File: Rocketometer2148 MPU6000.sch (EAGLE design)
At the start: 75 parts, among them J001 USB_MICROB_JST, J301 JST 2mm, J401 M06, J402 M06, J701 MICROSD-SOCKET, Q050 PMOS, Q201 PMOS, U101 BMP180, U201 5319, U301 73831, U401 LPC2148, U402 SN74LVC1G32, U501 L3G4200D, U801 5883, U901 LIS331, U902 AD377, Y401 12MHz, Y402 32kiHz

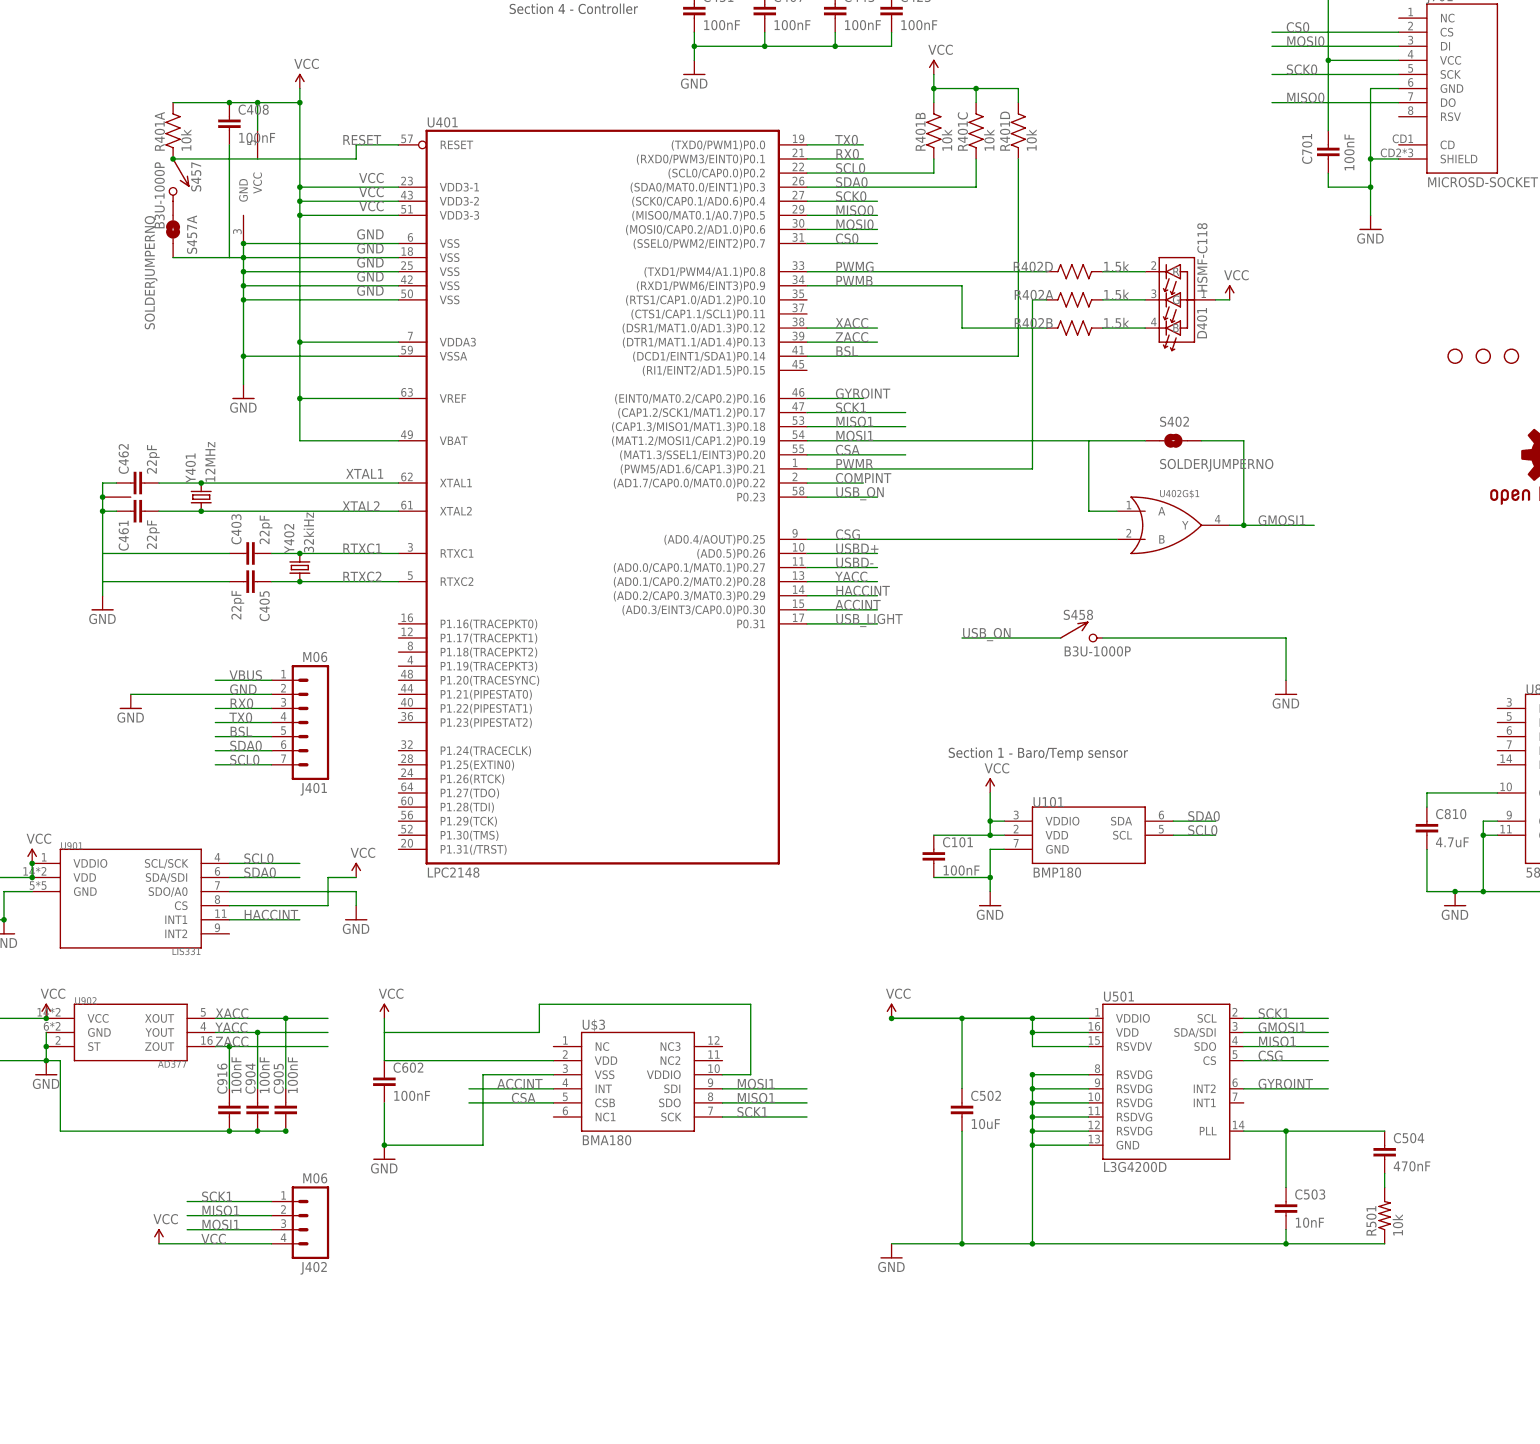
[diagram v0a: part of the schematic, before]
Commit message: Made 11DoF for BMA180, MPU6000, replaced ADXL345 with BMA180 in Rocketometer2148, made Rocketometer2148 with MPU6000
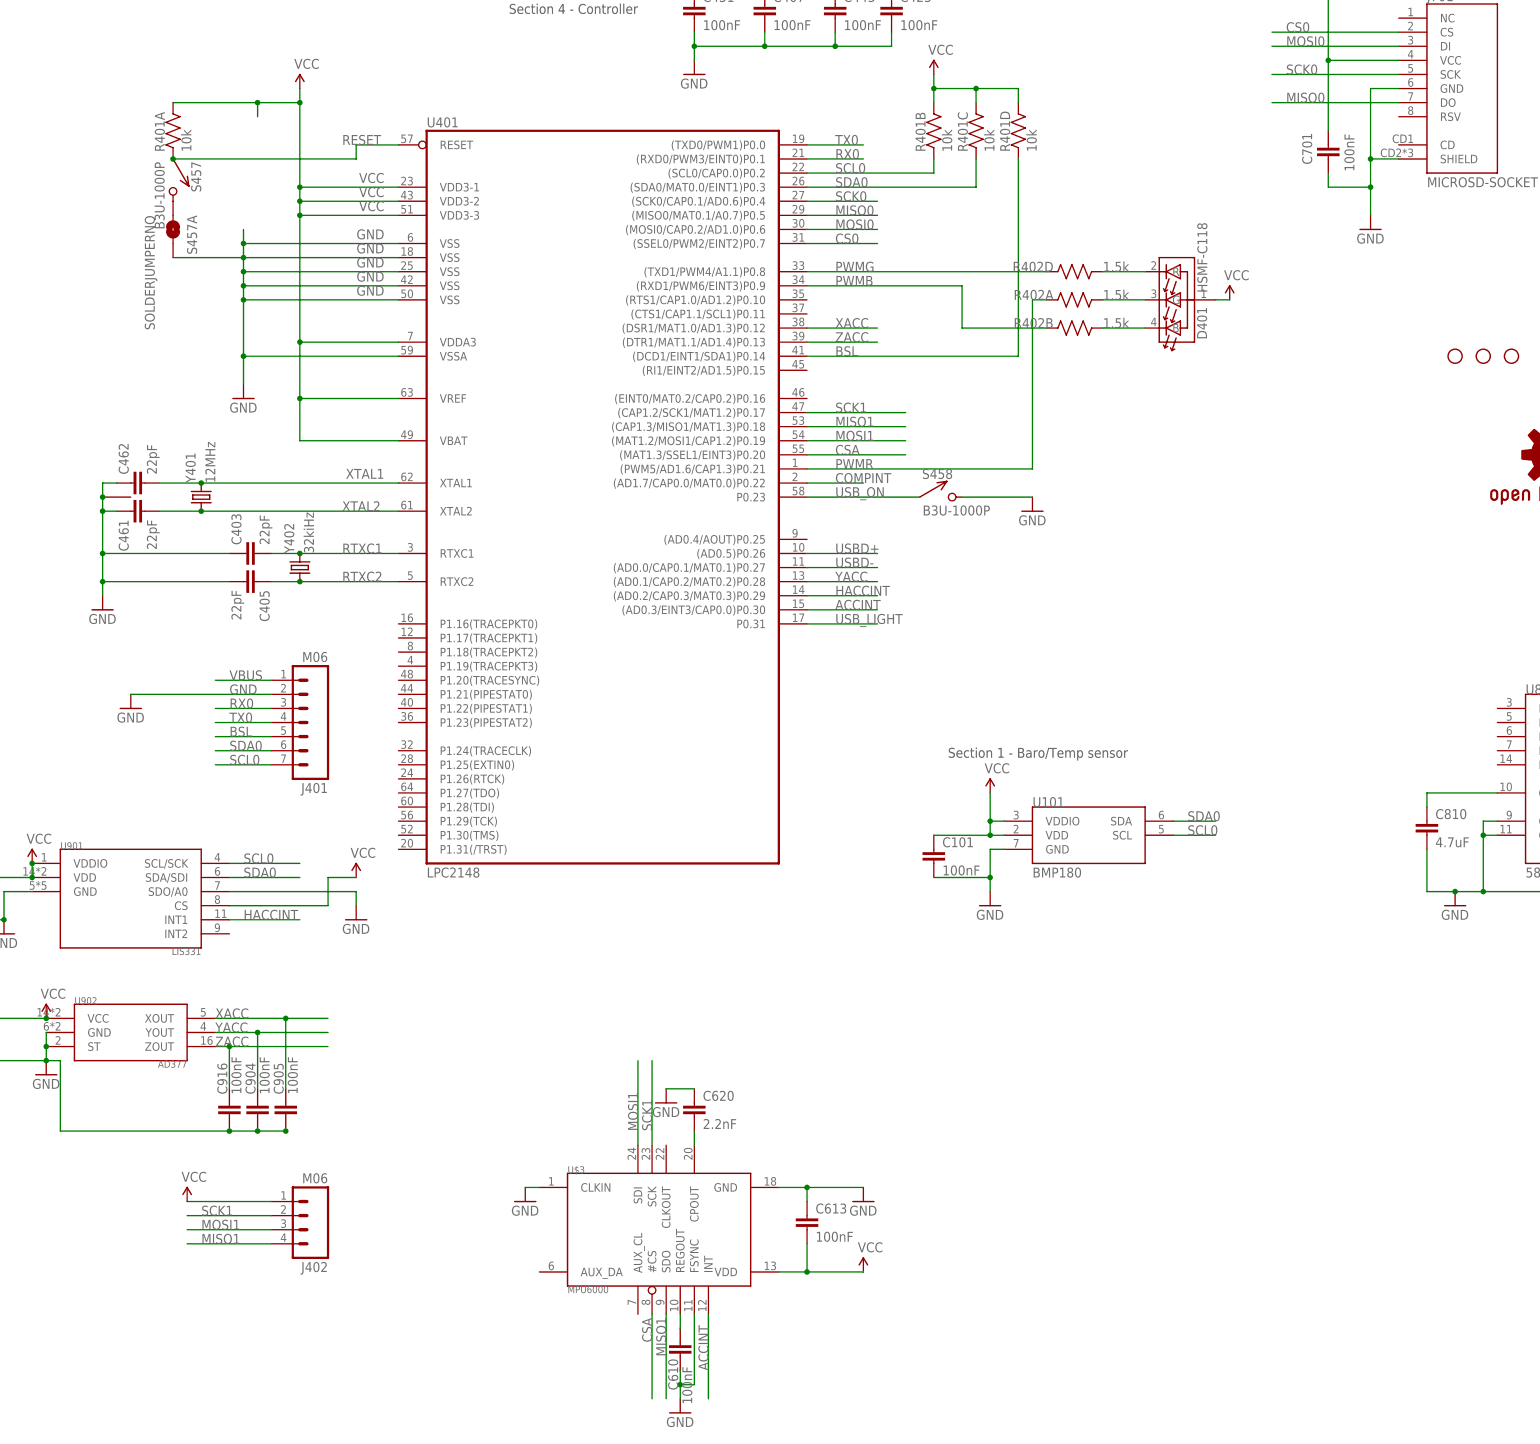
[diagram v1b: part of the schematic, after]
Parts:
- removed C408, C602: 100nF, SparkFun:CAP0402-CAP
- removed C502: 10uF, SparkFun:CAP0603-CAP
- removed C503: 10nF, SparkFun:CAP0402-CAP
- removed C504: 470nF, SparkFun:CAP0402-CAP
- removed R501: 10k, SparkFun:RESISTOR0402-RES
- removed S402: SOLDERJUMPERNO, SparkFun-Passives:SOLDERJUMPERNO
- removed U402: SN74LVC1G32, KwanSystems:SN74LVC1G32
- removed U501: L3G4200D, SparkFun:L3G4200D
- added C610, C613: 100nF, SparkFun:CAP0402-CAP
- added C620: 2.2nF, SparkFun:CAP0402-CAP
- D050: DIGIKEY 754-1434-1-ND -> 350-2037-1-ND
- D301: DIGIKEY 754-1354-1-ND -> 754-1124-1-ND
- U$3: value BMA180 -> MPU6000; device SparkFun-Sensors:BMA180 -> KwanSystems:MPU6000
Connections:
- removed net CSG: U401.(AD0.4/AOUT)P0.25, U402G$1.B, U501.CS
- removed net GMOSI1: S402.2, U402G$1.Y, U501.SDA/SDI
- removed net GYROINT: U401.(EINT0/MAT0.2/CAP0.2)P0.16, U501.INT2
- removed net N$20: C503.1, C504.1, U501.PLL
- new net N$13: C610.1, U$3.REGOUT
- net CSA: now also U$3.#CS; no longer U$3.CSB
- net GND: now also C610.2, C613.1, C620.1, U$3.CLKIN, U$3.FSYNC, U$3.GND; no longer C408.2, C502.2, C503.2, C602.2, R501.1, U$3.VSS, U402G$2.GND, U501.GND, U501.RSDVG@3, U501.RSVDG@0, U501.RSVDG@1, U501.RSVDG@2, U501.RSVDG@4
- net MISO1: now also J402.4; no longer J402.2, U501.SDO
- net MOSI1: no longer S402.1, U402G$1.A
- net N$1: now also C620.2, U$3.CPOUT; no longer C504.2, R501.2
- net SCK1: now also J402.2; no longer J402.1, U501.SCL
- net VCC: now also C613.2, J402.1; no longer C408.1, C502.1, C602.1, J402.4, U$3.VDDIO, U402G$2.VCC, U501.RSVDV@0, U501.VDD, U501.VDDIO
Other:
- moved on the sheet: S458

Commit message: Split off hardware stack initialization and checking
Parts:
- removed C904, C905, C916: 100nF, SparkFun:CAP0402-CAP
- removed C914: 4.7uF, SparkFun:CAP0402-CAP
- removed Q201: PMOS, SparkFun:MOSFET-PCHANNELSMD
- removed U902: AD377, KwanSystems:ADXL377
- added C449, C463: 100nF, SparkFun:CAP0402-CAP
- J401: device SparkFun-Connectors:M07 -> SparkFun-Connectors:M08LOCK
- J402: device SparkFun-Connectors:M04PTH -> SparkFun-Connectors:M04LOCK
- renumbered C201 to C215, C203 to C214
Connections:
- removed net RAW: C204.1, Q201.D, U201.EN, U201.VIN
- removed net XACC: C905.1, U401.(DSR1/MAT1.0/AD1.3)P0.12, U902.XOUT
- removed net YACC: C904.1, U401.(AD0.1/CAP0.2/MAT0.2)P0.28, U902.YOUT
- removed net ZACC: C916.1, U401.(DTR1/MAT1.1/AD1.4)P0.13, U902.ZOUT
- net BSL: now also J401.6; no longer J401.5
- net GND: now also C449.1, C463.2, J401.3, S201.S; no longer C904.2, C905.2, C914.2, C916.2, J401.2, S201.O, U902.GND, U902.ST
- net N$10: now also U201.EN; no longer Q201.G
- net RX0: now also J401.4; no longer J401.3
- net SCL0: now also J401.8; no longer J401.7
- net SDA0: now also J401.7; no longer J401.6
- net TX0: now also J401.5; no longer J401.4
- net VBUS: now also J401.2; no longer J401.1
- net VCC: now also C463.1; no longer C914.1, U401.VBAT, U902.VCC
- net VIN: now also C204.1, S201.O, U201.VIN; no longer Q201.S, S201.S
- net VLIPO: now also C449.2, J401.1, U401.VBAT
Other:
- moved on the sheet: R401A, S201, S457, S457A

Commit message: Finished routing of board
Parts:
- removed C901: 10uF, SparkFun:CAP0603-CAP
- removed U901: LIS331, KwanSystems:H3LIS331DL
- added C904, C905, C916: 100nF, SparkFun:CAP0402-CAP
- added C914: 4.7uF, SparkFun:CAP0402-CAP
- added U902: AD377, KwanSystems:ADXL377
- renumbered JP3 to JP5
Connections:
- new net XACC: C905.1, U401.(DSR1/MAT1.0/AD1.3)P0.12, U902.XOUT
- new net YACC: C904.1, U401.(AD0.1/CAP0.2/MAT0.2)P0.28, U902.YOUT
- new net ZACC: C916.1, U401.(DTR1/MAT1.1/AD1.4)P0.13, U902.ZOUT
- net GND: now also C904.2, C905.2, C914.2, C916.2, U902.GND, U902.ST; no longer C901.2, U901.GND, U901.SDO/A0
- net HACCINT: no longer U901.INT1
- net SCL0: no longer U901.SCL/SCK
- net SDA0: no longer U901.SDA/SDI
- net VCC: now also C914.1, U902.VCC; no longer C901.1, U901.CS, U901.VDD, U901.VDDIO

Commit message: Further cleanup of board
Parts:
- U801: value 5883 -> HMC5883L; LABEL_3D50 (none) -> 5883
- U902: value AD377 -> ADXL377
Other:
- note added: "For R301=10k, Ireg=1000V/10000Ohm=0.1A"
- note added: "Max charge current Ireg=1000V/R301"
- moved on the sheet: C204, C214, C215, D302, U201

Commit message: Flip card slot to opposite side of board, shorten board
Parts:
- removed C463, C701: 100nF, SparkFun:CAP0402-CAP
- C407, C423: value 100nF -> 1uF
- J401: device SparkFun-Connectors:M08LOCK -> SparkFun-Connectors:M07LOCK
- renumbered JP5 to JP3, U$3 to U601
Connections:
- net N$10 renamed PWR_EN
- net ACCINT: now also U401.(EINT0/MAT0.2/CAP0.2)P0.16; no longer U401.(AD0.3/EINT3/CAP0.0)P0.30
- net BSL: now also J401.5, R401A.1; no longer J401.6, R401D.1
- net CS0: now also U401.(PWM5/AD1.6/CAP1.3)P0.21; no longer U401.(SSEL0/PWM2/EINT2)P0.7
- net CSA: now also U401.(CTS1/CAP1.1/SCL1)P0.11; no longer U401.(MAT1.3/SSEL1/EINT3)P0.20
- net GND: now also J401.1; no longer C463.2, C701.2, J401.3
- net PWMR: now also U401.(SSEL0/PWM2/EINT2)P0.7; no longer U401.(PWM5/AD1.6/CAP1.3)P0.21
- net RESET: now also R401B.1; no longer R401A.1
- net SCL0: now also J401.7, R401D.1; no longer J401.8, R401B.1
- net SDA0: now also J401.6; no longer J401.7
- net TX0: now also J401.3; no longer J401.5
- net VCC: no longer C463.1, C701.1
- net VLIPO: no longer J401.1
- net YACC: now also U401.(RI1/EINT2/AD1.5)P0.15; no longer U401.(AD0.1/CAP0.2/MAT0.2)P0.28
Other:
- moved on the sheet: R401A, R401B, R401D

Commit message: Finished routing shorter board
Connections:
- net XACC: now also U401.(DTR1/MAT1.1/AD1.4)P0.13; no longer U401.(DSR1/MAT1.0/AD1.3)P0.12
- net ZACC: now also U401.(DSR1/MAT1.0/AD1.3)P0.12; no longer U401.(DTR1/MAT1.1/AD1.4)P0.13
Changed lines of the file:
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@@
 </segment>
 <segment>
-<pinref part="U401" gate="G$1" pin="(DSR1/MAT1.0/AD1.3)P0.12"/>
-<wire x1="149.86" y1="-73.66" x2="160.02" y2="-73.66" width="0.1524" layer="91"/>
-<label x="154.94" y="-73.66" size="1.778" layer="95"/>
+<pinref part="U401" gate="G$1" pin="(DTR1/MAT1.1/AD1.4)P0.13"/>
+<wire x1="149.86" y1="-76.2" x2="160.02" y2="-76.2" width="0.1524" layer="91"/>
+<label x="154.94" y="-76.2" size="1.778" layer="95"/>
 </segment>
 </net>
@@
 </segment>
 <segment>
-<pinref part="U401" gate="G$1" pin="(DTR1/MAT1.1/AD1.4)P0.13"/>
-<wire x1="149.86" y1="-76.2" x2="160.02" y2="-76.2" width="0.1524" layer="91"/>
-<label x="154.94" y="-76.2" size="1.778" layer="95"/>
+<pinref part="U401" gate="G$1" pin="(DSR1/MAT1.0/AD1.3)P0.12"/>
+<wire x1="149.86" y1="-73.66" x2="160.02" y2="-73.66" width="0.1524" layer="91"/>
+<label x="154.94" y="-73.66" size="1.778" layer="95"/>
 </segment>
 </net>

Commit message: RocketometerMPU sent to Laen
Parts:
- added JP4, JP5: STAND-OFFTIGHT, SparkFun-Electromechanical:STAND-OFFTIGHT
- J401: value M06 -> M07
- J402: value M06 -> M04
- U201: value 5319 -> MIC5319
- U301: value 73831 -> MCP73831
- renumbered C407 to C463
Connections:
- removed net HACCINT: U401.(AD0.2/CAP0.3/MAT0.3)P0.29
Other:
- moved on the sheet: C101, C610, C613, C620, C904, C905, C914, C916, J401, J402, U101, U601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

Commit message: Packaging for push
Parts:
- added C907: 100nF, SparkFun-Passives:CAP0402-CAP
- added C908: 10uF, SparkFun:CAP0603-CAP
- added U901: ADXL377, KwanSystems:ADXL377
- J401: device SparkFun-Connectors:M07LOCK -> SparkFun-Connectors:M07
- J402: device SparkFun-Connectors:M04LOCK -> SparkFun-Connectors:M04PTH
- U902: value ADXL377 -> AD7995; device KwanSystems:ADXL377 -> KwanSystems:AD799X; DIGIKEY (none) -> AD7995YRJZ-1500RL7CT-ND
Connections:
- net GND: now also C907.2, C908.2, J401.2, U901.GND, U901.ST; no longer J401.1, U902.ST
- net SCL0: now also U902.SCL
- net SDA0: now also U902.SDA
- net VBUS: now also J401.1; no longer J401.2
- net VCC: now also C907.1, C908.1, U901.VCC, U902.VDD; no longer U902.VCC
- net XACC: now also U901.XOUT, U902.VIN0; no longer U401.(DTR1/MAT1.1/AD1.4)P0.13, U902.XOUT
- net YACC: now also U901.YOUT, U902.VIN1; no longer U401.(RI1/EINT2/AD1.5)P0.15, U902.YOUT
- net ZACC: now also U901.ZOUT, U902.VIN3/VREF; no longer U401.(DSR1/MAT1.0/AD1.3)P0.12, U902.ZOUT
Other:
- moved on the sheet: C802, C808, C810, C904, C905, C914, C916, U801
